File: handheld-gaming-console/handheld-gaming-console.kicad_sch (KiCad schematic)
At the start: 0 parts

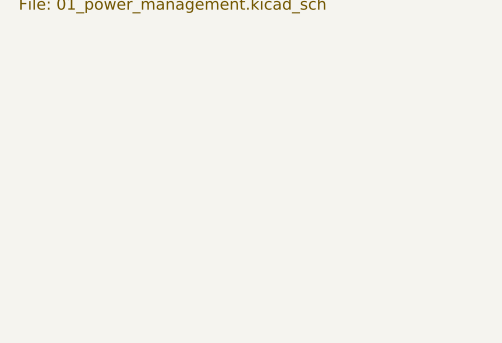
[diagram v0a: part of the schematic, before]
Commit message: feat(compute): route Core3566 DF40 peripheral connector and MASKROM recovery pin
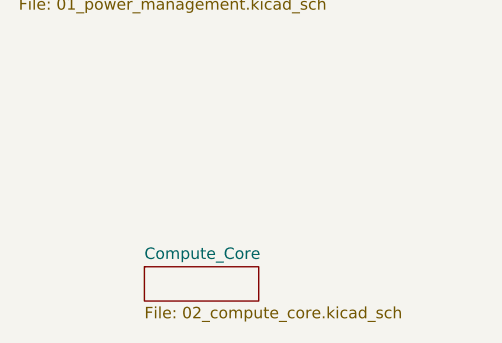
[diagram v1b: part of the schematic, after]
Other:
- added sheet Compute_Core (02_compute_core.kicad_sch)
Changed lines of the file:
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@@
+		)
+	)
+	(sheet
+		(at 67.31 114.3)
+		(size 12.7 3.81)
+		(exclude_from_sim no)
+		(in_bom yes)
+		(on_board yes)
+		(dnp no)
+		(fields_autoplaced yes)
+		(stroke
+			(width 0.1524)
+			(type solid)
+		)
+		(fill
+			(color 0 0 0 0)
+		)
+		(property "Sheetname" "Compute_Core"
+			(at 67.31 113.5884 0)
+			(show_name no)
+			(do_not_autoplace no)
+			(effects
+				(font
+					(size 1.27 1.27)
+				)
+				(justify left bottom)
+			)
+		)
+		(property "Sheetfile" "02_compute_core.kicad_sch"
+			(at 67.31 118.6946 0)
+			(show_name no)
+			(do_not_autoplace no)
+			(effects
+				(font
+					(size 1.27 1.27)
+				)
+				(justify left top)
+			)
+		)
+		(instances
+			(project "handheld-gaming-console"
+				(path "/888c448d-6c8e-4815-9453-39981fbb99f0"
+					(page "3")
+				)
+			)
 		)
 	)

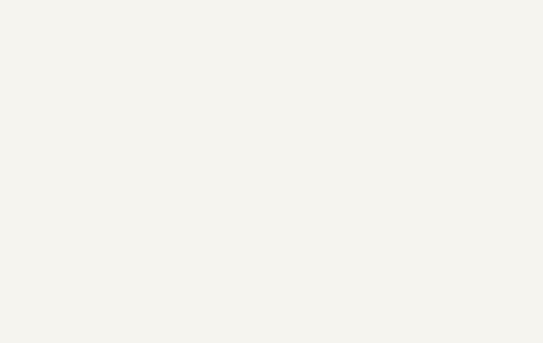
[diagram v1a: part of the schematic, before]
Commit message: feat(usb): implement USB2514B 4-port hub controller with crystal clocking and analog filtering
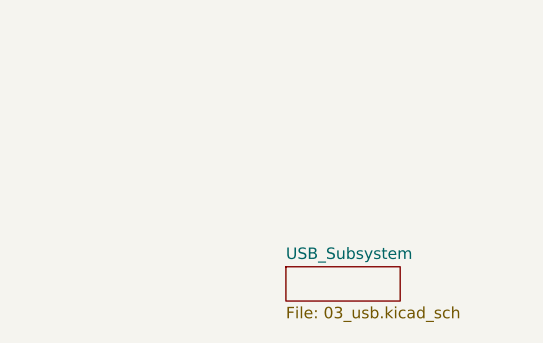
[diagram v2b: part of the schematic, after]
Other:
- added sheet USB_Subsystem (03_usb.kicad_sch)
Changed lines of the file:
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@@
+		)
+	)
+	(sheet
+		(at 95.25 171.45)
+		(size 12.7 3.81)
+		(exclude_from_sim no)
+		(in_bom yes)
+		(on_board yes)
+		(dnp no)
+		(fields_autoplaced yes)
+		(stroke
+			(width 0.1524)
+			(type solid)
+		)
+		(fill
+			(color 0 0 0 0)
+		)
+		(property "Sheetname" "USB_Subsystem"
+			(at 95.25 170.7384 0)
+			(show_name no)
+			(do_not_autoplace no)
+			(effects
+				(font
+					(size 1.27 1.27)
+				)
+				(justify left bottom)
+			)
+		)
+		(property "Sheetfile" "03_usb.kicad_sch"
+			(at 95.25 175.8446 0)
+			(show_name no)
+			(do_not_autoplace no)
+			(effects
+				(font
+					(size 1.27 1.27)
+				)
+				(justify left top)
+			)
+		)
+		(instances
+			(project "handheld-gaming-console"
+				(path "/888c448d-6c8e-4815-9453-39981fbb99f0"
+					(page "4")
+				)
+			)
 		)
 	)

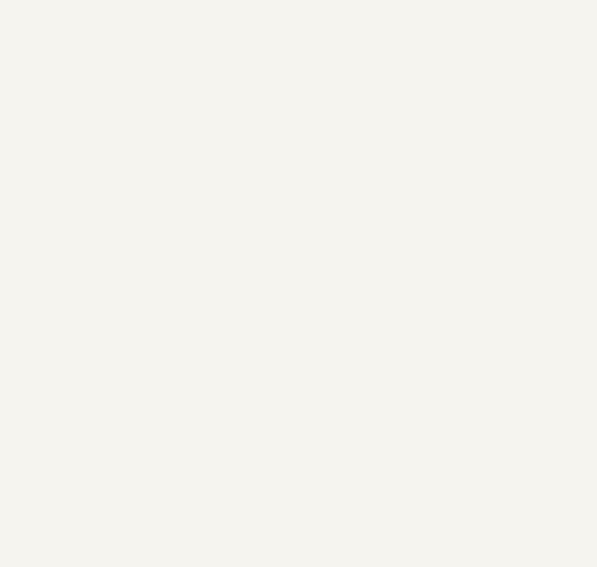
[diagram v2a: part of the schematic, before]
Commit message: feat(display): wire 15-pin FPC connector with MIPI-DSI lanes and touch I2C bus
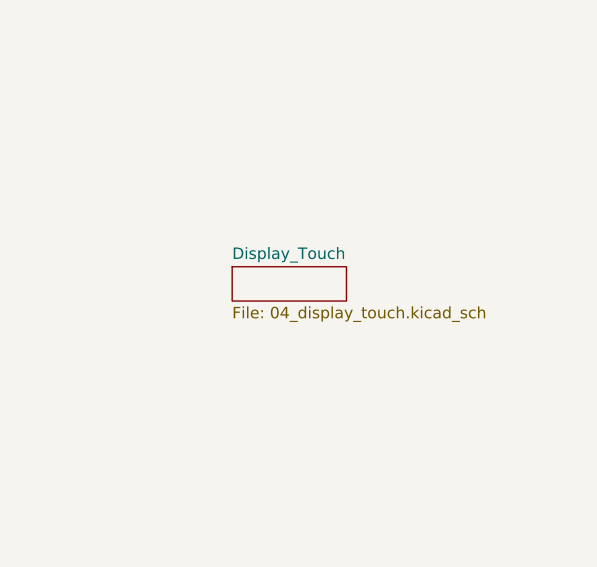
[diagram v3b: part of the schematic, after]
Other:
- added sheet Display_Touch (04_display_touch.kicad_sch)
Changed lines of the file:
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@@
+	)
+	(sheet
+		(at 187.96 120.65)
+		(size 12.7 3.81)
+		(exclude_from_sim no)
+		(in_bom yes)
+		(on_board yes)
+		(dnp no)
+		(fields_autoplaced yes)
+		(stroke
+			(width 0.1524)
+			(type solid)
+		)
+		(fill
+			(color 0 0 0 0)
+		)
+		(property "Sheetname" "Display_Touch"
+			(at 187.96 119.9384 0)
+			(show_name no)
+			(do_not_autoplace no)
+			(effects
+				(font
+					(size 1.27 1.27)
+				)
+				(justify left bottom)
+			)
+		)
+		(property "Sheetfile" "04_display_touch.kicad_sch"
+			(at 187.96 125.0446 0)
+			(show_name no)
+			(do_not_autoplace no)
+			(effects
+				(font
+					(size 1.27 1.27)
+				)
+				(justify left top)
+			)
+		)
+		(instances
+			(project "handheld-gaming-console"
+				(path "/888c448d-6c8e-4815-9453-39981fbb99f0"
+					(page "5")
+				)
+			)
+		)
 	)
 	(sheet

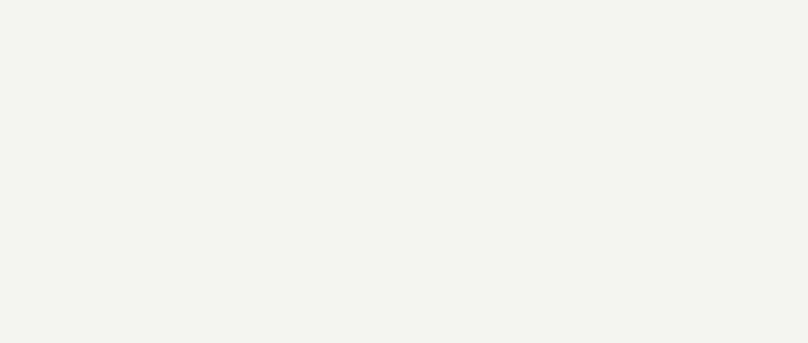
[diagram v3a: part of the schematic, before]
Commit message: feat(gamepad): wire RP2040 MCU core, crystal oscillator, 4MB flash, and impedance-matched USB
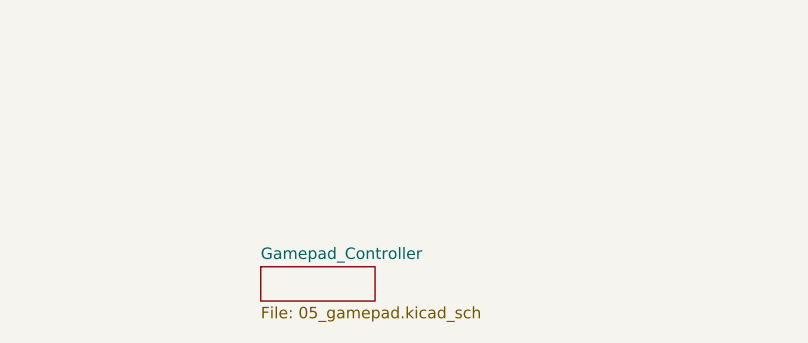
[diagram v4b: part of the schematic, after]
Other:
- added sheet Gamepad_Controller (05_gamepad.kicad_sch)
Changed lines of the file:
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@@
+	)
+	(sheet
+		(at 167.64 172.72)
+		(size 12.7 3.81)
+		(exclude_from_sim no)
+		(in_bom yes)
+		(on_board yes)
+		(dnp no)
+		(fields_autoplaced yes)
+		(stroke
+			(width 0.1524)
+			(type solid)
+		)
+		(fill
+			(color 0 0 0 0)
+		)
+		(property "Sheetname" "Gamepad_Controller"
+			(at 167.64 172.0084 0)
+			(show_name no)
+			(do_not_autoplace no)
+			(effects
+				(font
+					(size 1.27 1.27)
+				)
+				(justify left bottom)
+			)
+		)
+		(property "Sheetfile" "05_gamepad.kicad_sch"
+			(at 167.64 177.1146 0)
+			(show_name no)
+			(do_not_autoplace no)
+			(effects
+				(font
+					(size 1.27 1.27)
+				)
+				(justify left top)
+			)
+		)
+		(instances
+			(project "handheld-gaming-console"
+				(path "/888c448d-6c8e-4815-9453-39981fbb99f0"
+					(page "6")
+				)
+			)
+		)
 	)
 	(sheet

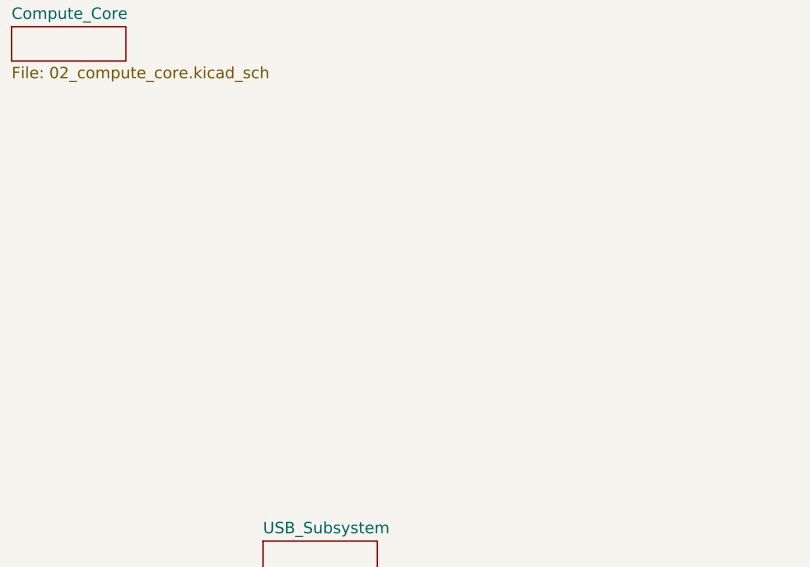
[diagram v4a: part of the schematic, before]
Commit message: feat(audio): tap I2S bus from Core3566 and implement isolated MAX98357A Class-D speaker amplifier
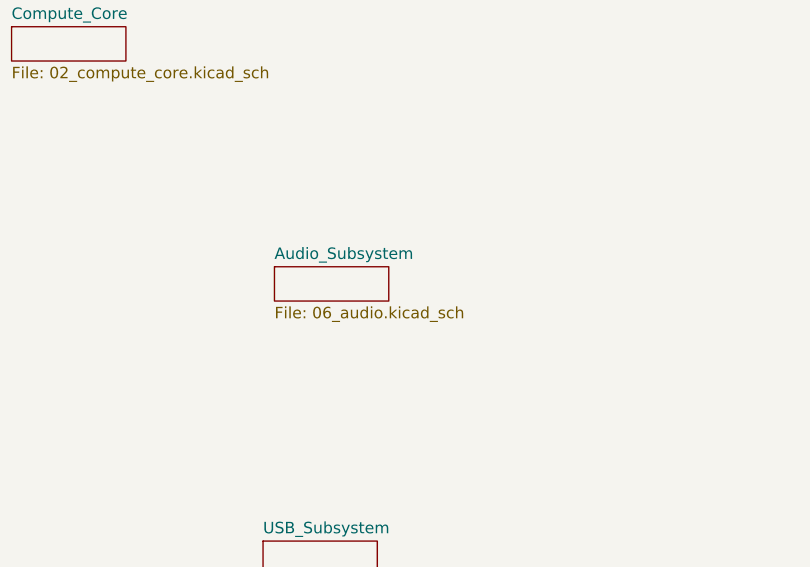
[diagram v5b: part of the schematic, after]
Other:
- added sheet Audio_Subsystem (06_audio.kicad_sch)
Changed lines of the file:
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@@
+	)
+	(sheet
+		(at 96.52 140.97)
+		(size 12.7 3.81)
+		(exclude_from_sim no)
+		(in_bom yes)
+		(on_board yes)
+		(dnp no)
+		(fields_autoplaced yes)
+		(stroke
+			(width 0.1524)
+			(type solid)
+		)
+		(fill
+			(color 0 0 0 0)
+		)
+		(property "Sheetname" "Audio_Subsystem"
+			(at 96.52 140.2584 0)
+			(show_name no)
+			(do_not_autoplace no)
+			(effects
+				(font
+					(size 1.27 1.27)
+				)
+				(justify left bottom)
+			)
+		)
+		(property "Sheetfile" "06_audio.kicad_sch"
+			(at 96.52 145.3646 0)
+			(show_name no)
+			(do_not_autoplace no)
+			(effects
+				(font
+					(size 1.27 1.27)
+				)
+				(justify left top)
+			)
+		)
+		(instances
+			(project "handheld-gaming-console"
+				(path "/888c448d-6c8e-4815-9453-39981fbb99f0"
+					(page "7")
+				)
+			)
+		)
 	)
 	(sheet
